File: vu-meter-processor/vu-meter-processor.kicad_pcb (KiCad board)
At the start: 2 copper layers, 53 x 94 mm, 78 parts, among them J1 SPI, J2 L, J3 R, J4 +5V, J6 +3.3V, U1 LM2904, U2 LM2904, U3 CH32X035F7P6, U4 DPU01L-15

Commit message: fix: change overall power supply to only 5V, make peak detector DNP for now
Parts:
- removed D4, D6: 4148, Diode_SMD:D_MiniMELF
- removed FB1: ~, Inductor_SMD:L_0603_1608Metric
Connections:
- C15 pad 2: GNDD -> GNDA
- C16 pad 2: GNDD -> GNDA
- C19 pad 2: GNDD -> GNDA
- C20 pad 2: GNDD -> GNDA
- D10 pad 2: GNDD -> GNDA
- D9 pad 2: GNDD -> GNDA
- H1 pad 1: GNDD -> GNDA
- H2 pad 1: GNDD -> GNDA
- J1 pad 5: GNDD -> GNDA
- J4 pad 2: GNDD -> GNDA
- JP1 pad 3: Net-(D4-K) -> Net-(D1-A)
- JP2 pad 3: Net-(D6-K) -> Net-(D5-A)
- TP3 pad 1: GNDD -> GNDA
- U3 pad 15: GNDD -> GNDA
- U4 pad 2: GNDD -> GNDA
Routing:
- net Net-(D1-A): track 7.55 -> 35.6 mm
- net Net-(D5-A): track 7.55 -> 35.5 mm
- net Net-(D4-K): track 26.6 -> 0.00 mm
- net Net-(D6-K): track 26.5 -> 0.00 mm
- net GNDA: track 7.14 -> 10.0 mm
- net GNDD: track 15.4 -> 13.7 mm
- removed copper zone on F.Cu, net GNDD

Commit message: remove analog peak detector fully and split one chip into two for better inter-channel performance
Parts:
- removed C12, C22: 0.1u, Capacitor_SMD:C_0805_2012Metric
- removed C13, C14: 1u, Capacitor_THT:CP_Radial_D4.0mm_P1.50mm
- removed C20: 220u, Capacitor_THT:CP_Radial_D8.0mm_P3.50mm
- removed D1, D2, D3, D5, D7, D8: 4148, Diode_SMD:D_MiniMELF
- removed D10: 5.1V, Diode_SMD:D_MiniMELF
- removed JP1: L Input, Jumper:SolderJumper-3_P1.3mm_Open_Pad1.0x1.5mm
- removed JP2: R Input, Jumper:SolderJumper-3_P1.3mm_Open_Pad1.0x1.5mm
- removed R13, R14, R18, R19: 47k, Resistor_SMD:R_0805_2012Metric
- removed R15, R20: 1k, Resistor_SMD:R_0805_2012Metric
- removed TP1: SWCLK, TestPoint:TestPoint_Pad_D2.0mm
- removed TP3: GNDD, TestPoint:TestPoint_Pad_D2.0mm
- removed TP4: SWDIO, TestPoint:TestPoint_Pad_D2.0mm
- removed TP5: 5V, TestPoint:TestPoint_Pad_D2.0mm
- removed U2: LM2904, Package_SO:SOP-8_3.9x4.9mm_P1.27mm
- added C23: 0.1u, Capacitor_SMD:C_0805_2012Metric, F.Cu at (82.8, 85.0)
- added C24: 0.1u, Capacitor_SMD:C_0805_2012Metric, F.Cu at (74.8, 92.0)
- added D12: 5.1V, Diode_SMD:D_MiniMELF, F.Cu at (78.8, 91.2)
- added J5: SPI R, Connector_JST:JST_XH_B5B-XH-A_1x05_P2.50mm_Vertical, B.Cu at (87.0, 82.8)
- added J7: SWD R, Connector_PinHeader_2.54mm:PinHeader_1x03_P2.54mm_Vertical, B.Cu at (76.7, 80.8)
- added U5: CH32X035F7P6, Package_SO:TSSOP-20_4.4x6.5mm_P0.65mm, F.Cu at (77.2, 86.5)
- J1: value SPI -> SPI L
- J6: value +3.3V -> SWD L; footprint Connector_JST:JST_XH_B2B-XH-A_1x02_P2.50mm_Vertical -> Connector_PinHeader_2.54mm:PinHeader_1x03_P2.54mm_Vertical
- moved REF** 69.9 mm to (57.8, 116.2), turned to 90 degrees
- moved REF** 57.2 mm to (57.8, 105.5)
- moved J6 31.0 mm to (60.0, 80.8), turned to -90 degrees
- moved H1 25.0 mm to (56.0, 74.0)
- moved H2 25.0 mm to (101.0, 74.0)
- moved C16 24.0 mm to (58.0, 92.0), turned to -90 degrees
- moved J1 22.3 mm to (70.2, 82.8), turned to -90 degrees
- moved U3 20.7 mm to (60.5, 86.5), turned to 0 degrees
- moved C15 20.6 mm to (66.0, 85.0), turned to 90 degrees
- moved R16 20.3 mm to (70.2, 102.2), turned to -90 degrees
- moved R21 20.3 mm to (80.8, 102.2), turned to -90 degrees
- moved D9 18.2 mm to (62.0, 91.5), turned to 0 degrees
- moved RV2 17.6 mm to (80.8, 99.5)
- moved RV1 17.6 mm to (70.2, 99.5)
- moved R17 14.1 mm to (65.2, 103.0)
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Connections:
- net LATCH renamed LATCH_L
- net MOSI renamed MOSI_L
- net SCK renamed SCK_L
- C10 pad 2: Net-(D5-A) -> Net-(C10-Pad2)
- C5 pad 2: Net-(D1-A) -> Net-(C5-Pad2)
- J6 pad 1: +5V -> Net-(J6-Pin_1)
- J6 pad 2: GNDD -> Net-(J6-Pin_2)
- R16 pad 2: Net-(JP1-C) -> Net-(C5-Pad2)
- R21 pad 2: Net-(JP2-C) -> Net-(C10-Pad2)
- U3 pad 19: Net-(U3-PC18/SWDIO) -> Net-(J6-Pin_1)
- U3 pad 20: Net-(U3-PC19/SWCLK) -> Net-(J6-Pin_2)
- U3 pad 7: R -> unconnected-(U3-PA1-Pad7)
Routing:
- net Net-(D1-A): track 35.6 -> 0.00 mm
- net Net-(D5-A): track 35.5 -> 0.00 mm
- net -15V: track 137.0 -> 112.1 mm
- net +5V: track 92.1 -> 68.9 mm
- net +15V: track 47.1 -> 31.5 mm
- net Net-(D5-K): track 15.3 -> 0.00 mm
- net Net-(D1-K): track 15.3 -> 0.00 mm
- net GNDD: track 13.7 -> 0.00 mm
- net Net-(JP1-A): track 13.3 -> 0.00 mm
- net Net-(JP2-A): track 13.2 -> 0.00 mm
- net Net-(D2-A): track 9.56 -> 0.00 mm
- net Net-(D7-K): track 8.19 -> 0.00 mm
- net Net-(D7-A): track 8.16 -> 0.00 mm
- net Net-(U3-PC18/SWDIO): track 8.14 -> 0.00 mm
- net Net-(U5-PC3/RST): track 0.00 -> 8.03 mm
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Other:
- board size 53 x 94 mm -> 53 x 69 mm

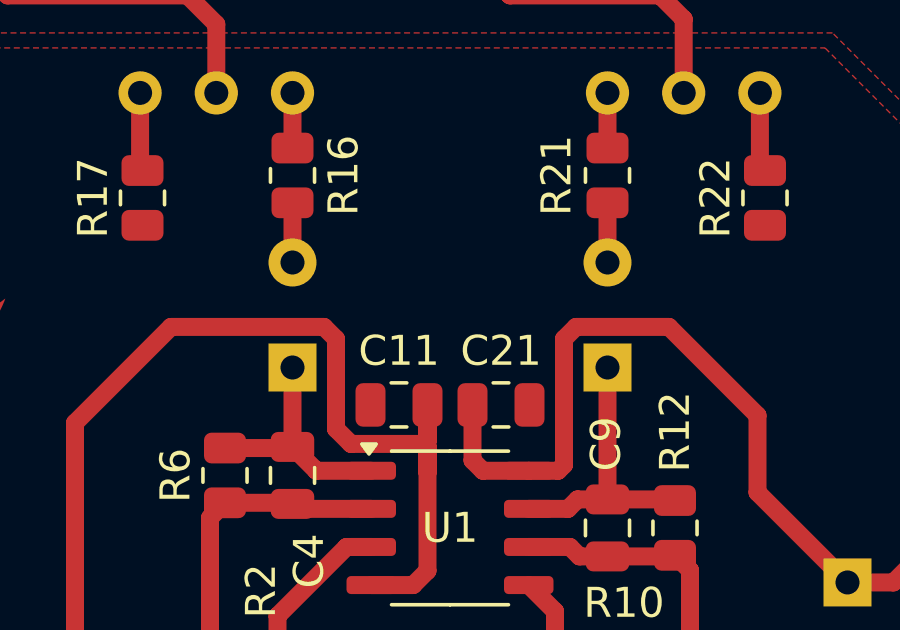
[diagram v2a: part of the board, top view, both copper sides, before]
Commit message: fix: remove dc blocking capacitors
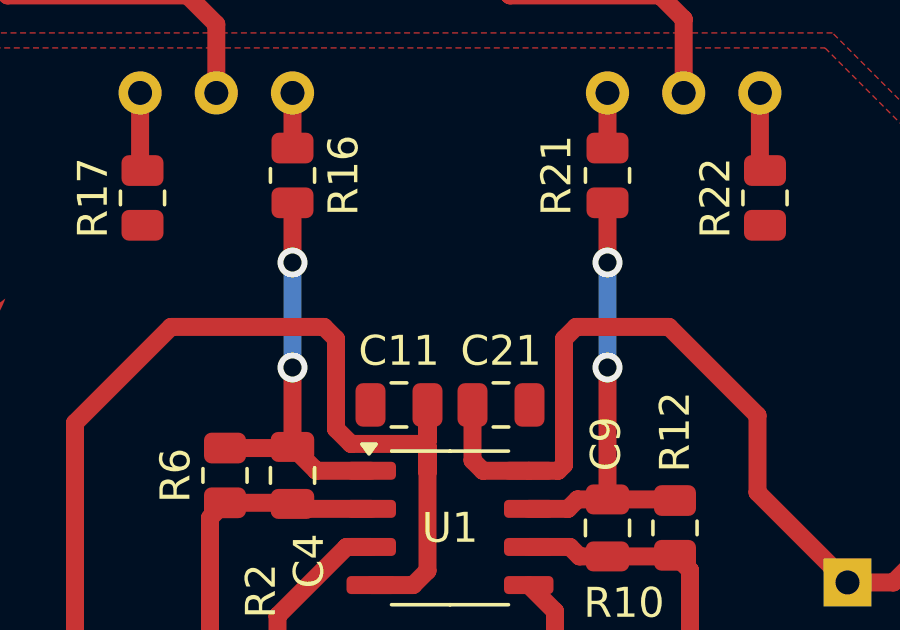
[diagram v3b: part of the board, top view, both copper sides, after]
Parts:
- removed C10, C5: 220u, Capacitor_THT:CP_Radial_D8.0mm_P3.50mm
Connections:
- C9 pad 2: Net-(C10-Pad1) -> Net-(C9-Pad2)
- R12 pad 2: Net-(C10-Pad1) -> Net-(C9-Pad2)
- R16 pad 2: Net-(C5-Pad2) -> Net-(C4-Pad2)
- R21 pad 2: Net-(C10-Pad2) -> Net-(C9-Pad2)
- U1 pad 7: Net-(C10-Pad1) -> Net-(C9-Pad2)
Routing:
- net Net-(C9-Pad2): track 0.00 -> 14.9 mm, vias 0 -> 2
- net Net-(C10-Pad1): track 9.42 -> 0.00 mm
- net Net-(C4-Pad2): track 7.87 -> 13.4 mm, vias 0 -> 2
- net Net-(C5-Pad2): track 1.99 -> 0.00 mm
- net Net-(C10-Pad2): track 1.99 -> 0.00 mm
